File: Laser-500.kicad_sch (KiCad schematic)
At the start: 10 parts, among them Q1 9018G, U1 Z80CPU, U2 74LS257, U3 74LS257, U4 74LS244, U5 27128, U6 27128, U7 74LS273, U8 2764, U9 74LS00

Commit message: RAM4164
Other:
- added sheet RAM (ram.kicad_sch)
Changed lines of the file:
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@@
+		)
+	)
+	(sheet
+		(at 37.592 25.146)
+		(size 34.798 19.812)
+		(fields_autoplaced yes)
+		(stroke
+			(width 0.1524)
+			(type solid)
+		)
+		(fill
+			(color 0 0 0 0.0000)
+		)
+		(property "Sheetname" "RAM"
+			(at 37.592 24.4344 0)
+			(effects
+				(font
+					(size 1.27 1.27)
+				)
+				(justify left bottom)
+			)
+		)
+		(property "Sheetfile" "ram.kicad_sch"
+			(at 37.592 45.5426 0)
+			(effects
+				(font
+					(size 1.27 1.27)
+				)
+				(justify left top)
+			)
+		)
+		(instances
+			(project "Laser-500"
+				(path "/c1a6b1ae-77c2-4767-93cc-3749547878e9"
+					(page "2")
+				)
+			)
 		)
 	)

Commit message: First Draft - RAM
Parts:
- removed Q1: 9018G, symbol Device:Q_NPN_EBC
- removed U1: Z80CPU, symbol CPU:Z80CPU
- removed U2, U3: 74LS257, symbol 74xx:74LS257
- removed U4: 74LS244, symbol 74xx:74LS244
- removed U5, U6: 27128, Package_DIP:DIP-28_W15.24mm, symbol Memory_EPROM:27128
- removed U7: 74LS273, symbol 74xx:74LS273
- removed U8: 2764, Package_DIP:DIP-28_W15.24mm, symbol Memory_EPROM:2764
- removed U9: 74LS00, symbol 74xx:74LS00
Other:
- added sheet CPU and ROM (cpu_main.kicad_sch)

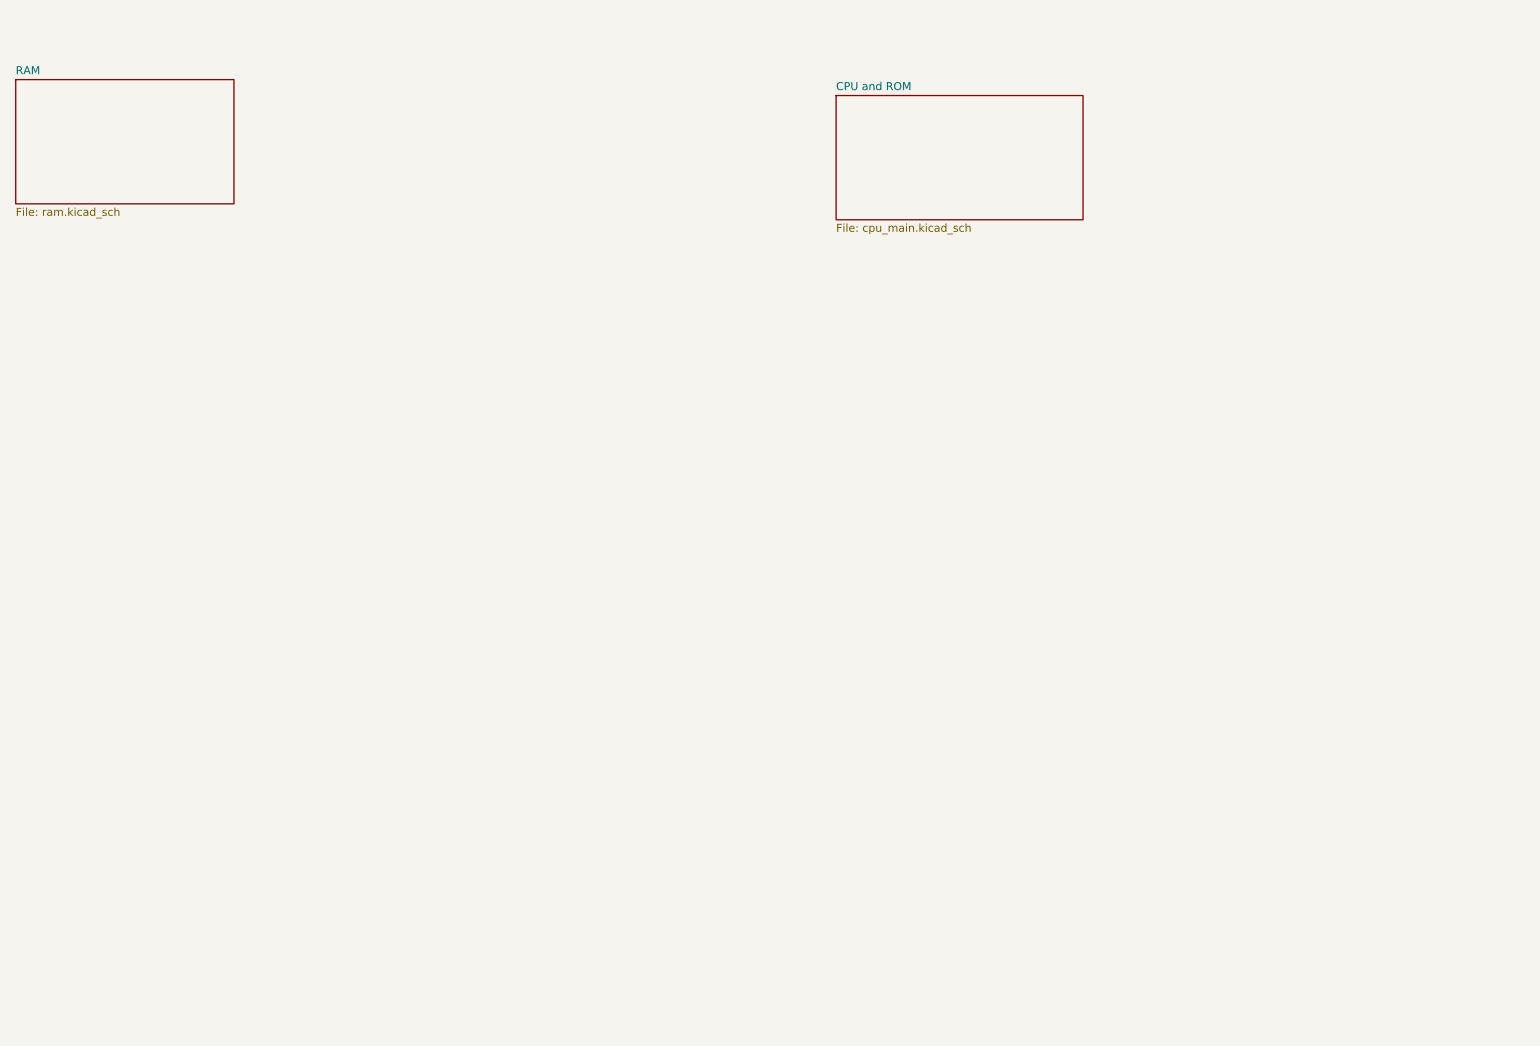
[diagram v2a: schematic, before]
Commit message: Started video_cassette sch
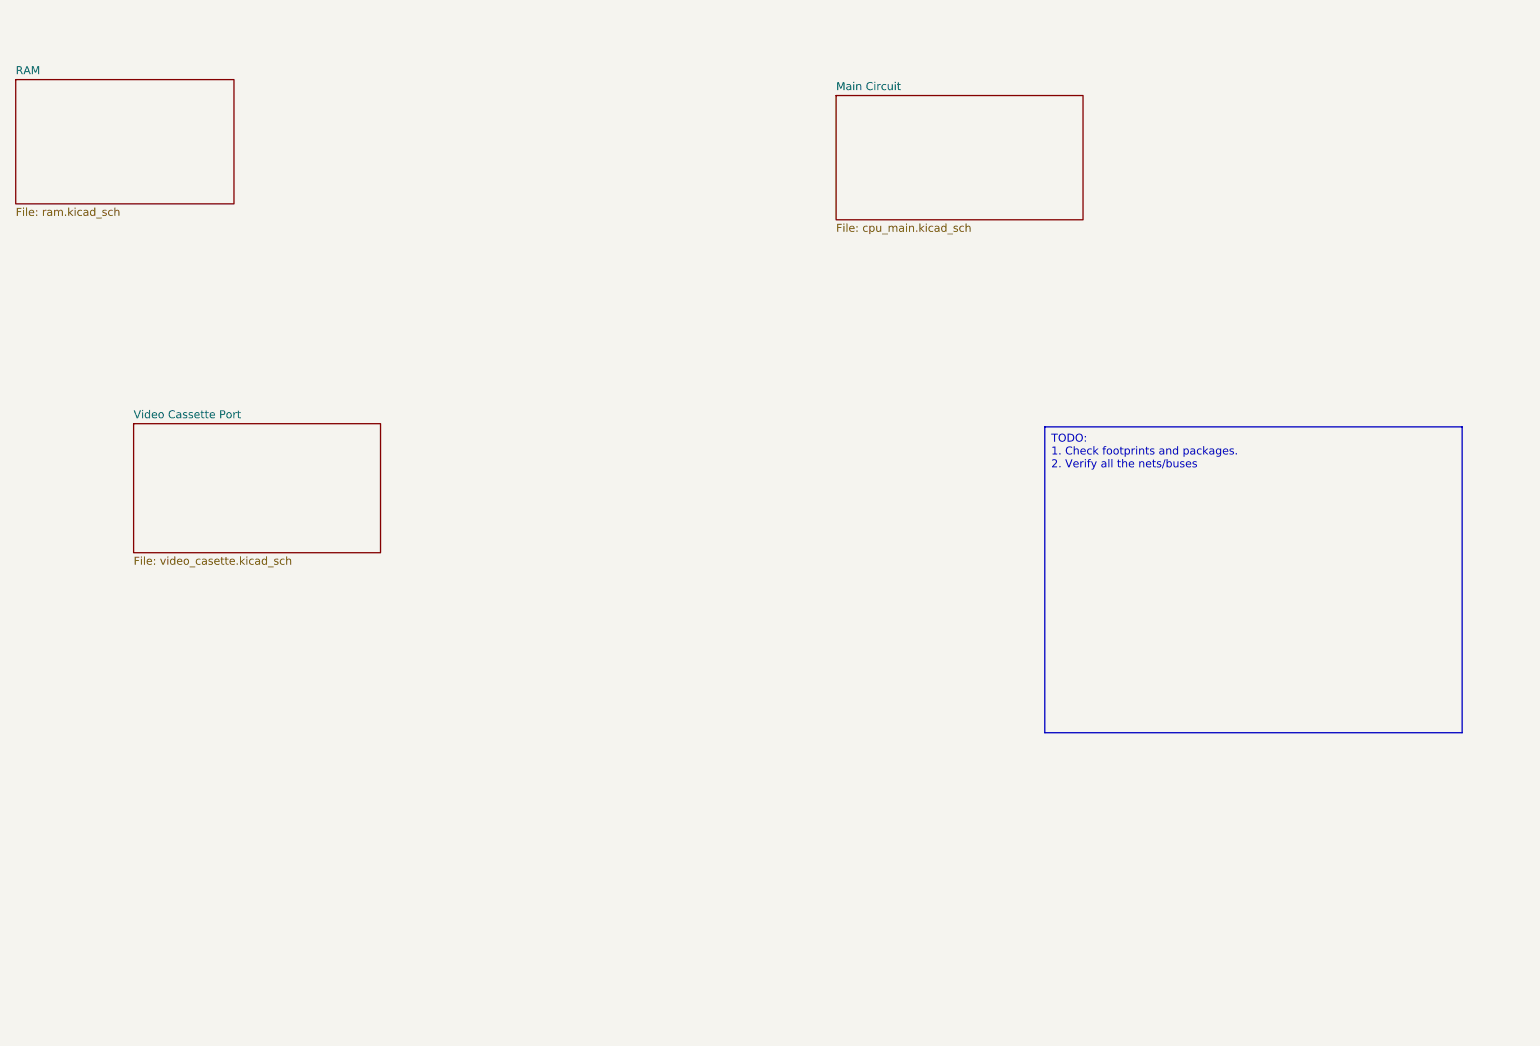
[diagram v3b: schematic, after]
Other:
- sheet CPU and ROM renamed Main Circuit
- added sheet Video Cassette Port (video_casette.kicad_sch)
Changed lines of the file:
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@@
 	(generator_version "8.0")
 	(paper "A4")
+	(text_box "TODO:\n1. Check footprints and packages.\n2. Verify all the nets/buses"
+		(exclude_from_sim no)
+		(at 201.676 80.518 0)
+		(size 66.548 48.768)
+		(stroke
+			(width 0)
+			(type default)
+		)
+		(fill
+			(type none)
+		)
+		(effects
+			(font
+				(size 1.27 1.27)
+			)
+			(justify left top)
+		)
+	)
 	(sheet
 		(at 37.592 25.146)
@@
 	)
 	(sheet
+		(at 56.388 80.01)
+		(size 39.37 20.574)
+		(fields_autoplaced yes)
+		(stroke
+			(width 0.1524)
+			(type solid)
+		)
+		(fill
+			(color 0 0 0 0.0000)
+		)
+		(property "Sheetname" "Video Cassette Port"
+			(at 56.388 79.2984 0)
+			(effects
+				(font
+					(size 1.27 1.27)
+				)
+				(justify left bottom)
+			)
+		)
+		(property "Sheetfile" "video_casette.kicad_sch"
+			(at 56.388 101.1686 0)
+			(effects
+				(font
+					(size 1.27 1.27)
+				)
+				(justify left top)
+			)
+		)
+		(instances
+			(project "Laser-500"
+				(path "/c1a6b1ae-77c2-4767-93cc-3749547878e9"
+					(page "4")
+				)
+			)
+		)
+	)
+	(sheet
 		(at 168.402 27.686)
 		(size 39.37 19.812)
@@
 			(color 0 0 0 0.0000)
 		)
-		(property "Sheetname" "CPU and ROM"
+		(property "Sheetname" "Main Circuit"
 			(at 168.402 26.9744 0)
 			(effects

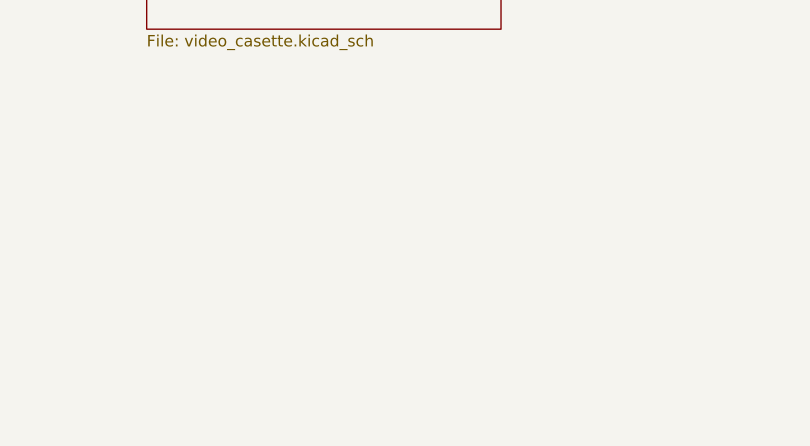
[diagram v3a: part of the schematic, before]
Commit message: A few Boxing day updates
1. Add Laser 500 Mainboard PCB photo
2. Updated Main circuit ICs and their symbols.
3. Updated references according to PCB photo
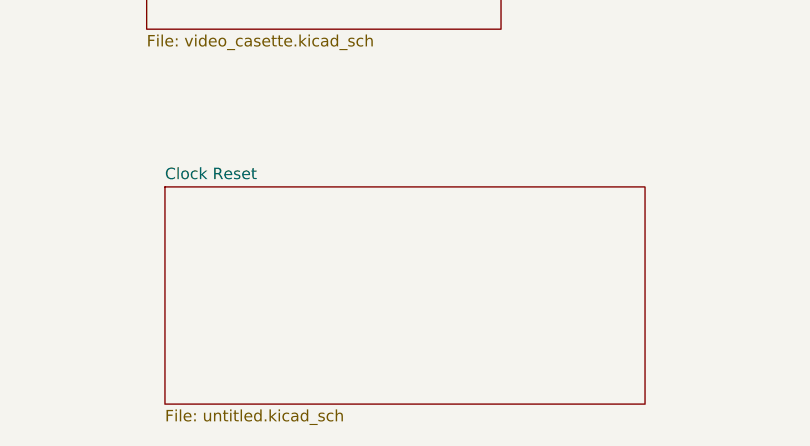
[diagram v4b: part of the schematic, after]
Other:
- added sheet Clock Reset (untitled.kicad_sch)
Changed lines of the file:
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@@
+	)
+	(sheet
+		(at 58.42 118.11)
+		(size 53.34 24.13)
+		(fields_autoplaced yes)
+		(stroke
+			(width 0.1524)
+			(type solid)
+		)
+		(fill
+			(color 0 0 0 0.0000)
+		)
+		(property "Sheetname" "Clock Reset"
+			(at 58.42 117.3984 0)
+			(effects
+				(font
+					(size 1.27 1.27)
+				)
+				(justify left bottom)
+			)
+		)
+		(property "Sheetfile" "untitled.kicad_sch"
+			(at 58.42 142.8246 0)
+			(effects
+				(font
+					(size 1.27 1.27)
+				)
+				(justify left top)
+			)
+		)
+		(instances
+			(project "Laser-500"
+				(path "/c1a6b1ae-77c2-4767-93cc-3749547878e9"
+					(page "5")
+				)
+			)
+		)
 	)
 	(sheet

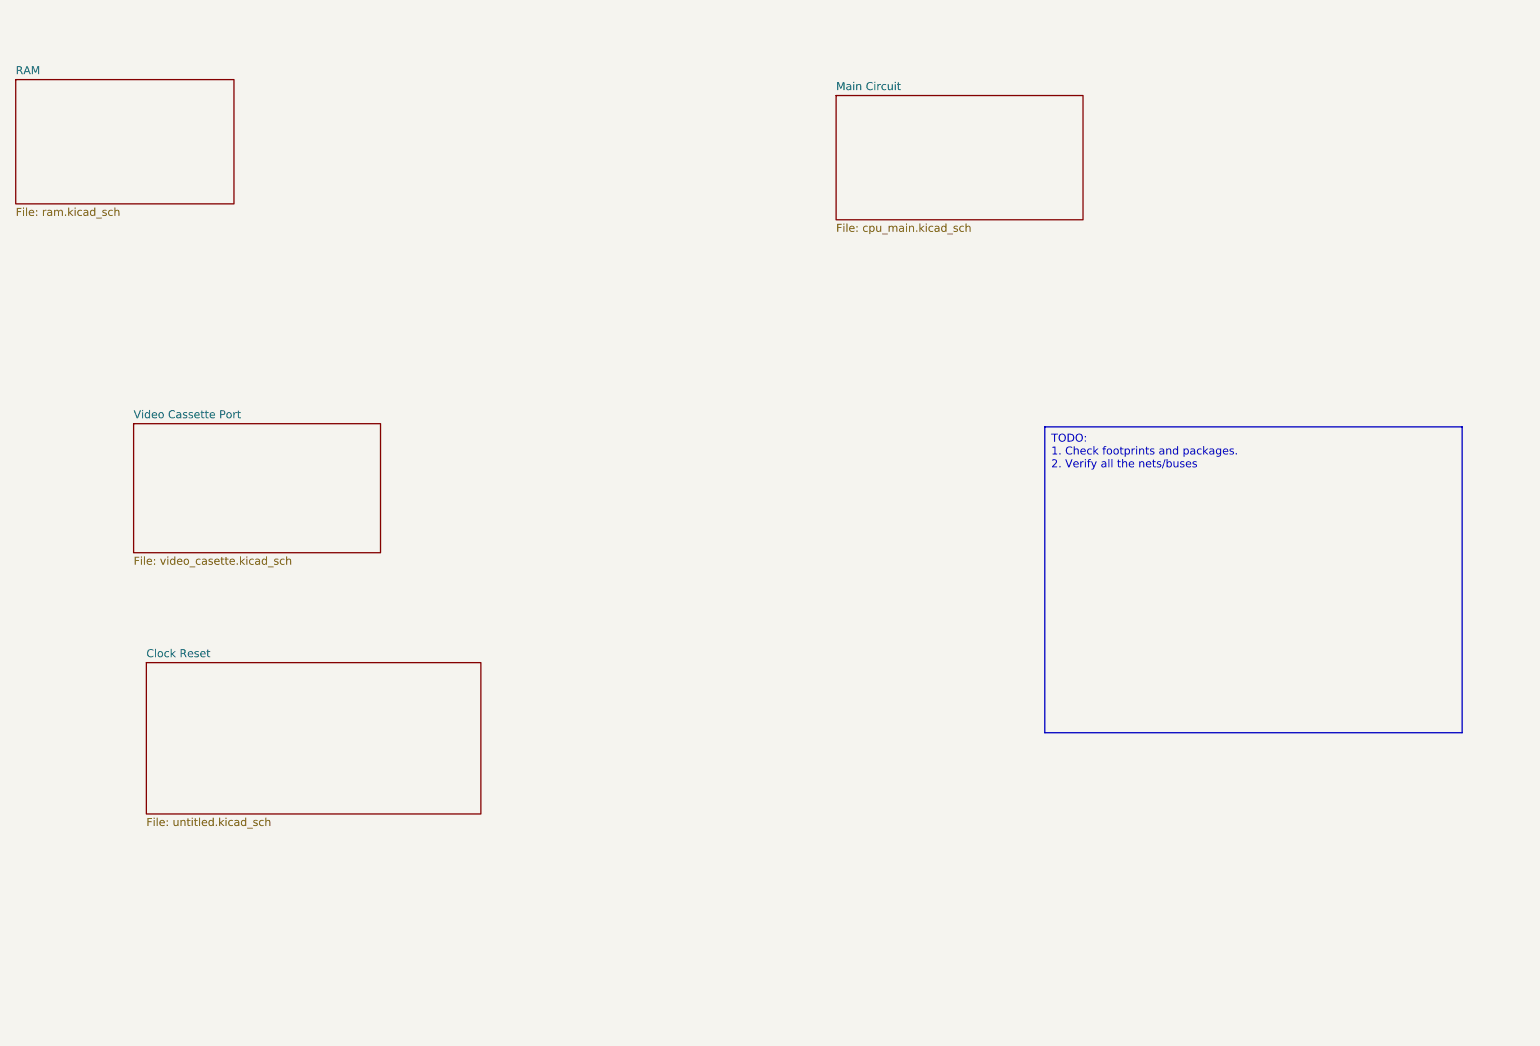
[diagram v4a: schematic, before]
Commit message: Started A[0..15] and MA[0..7] on main circuit
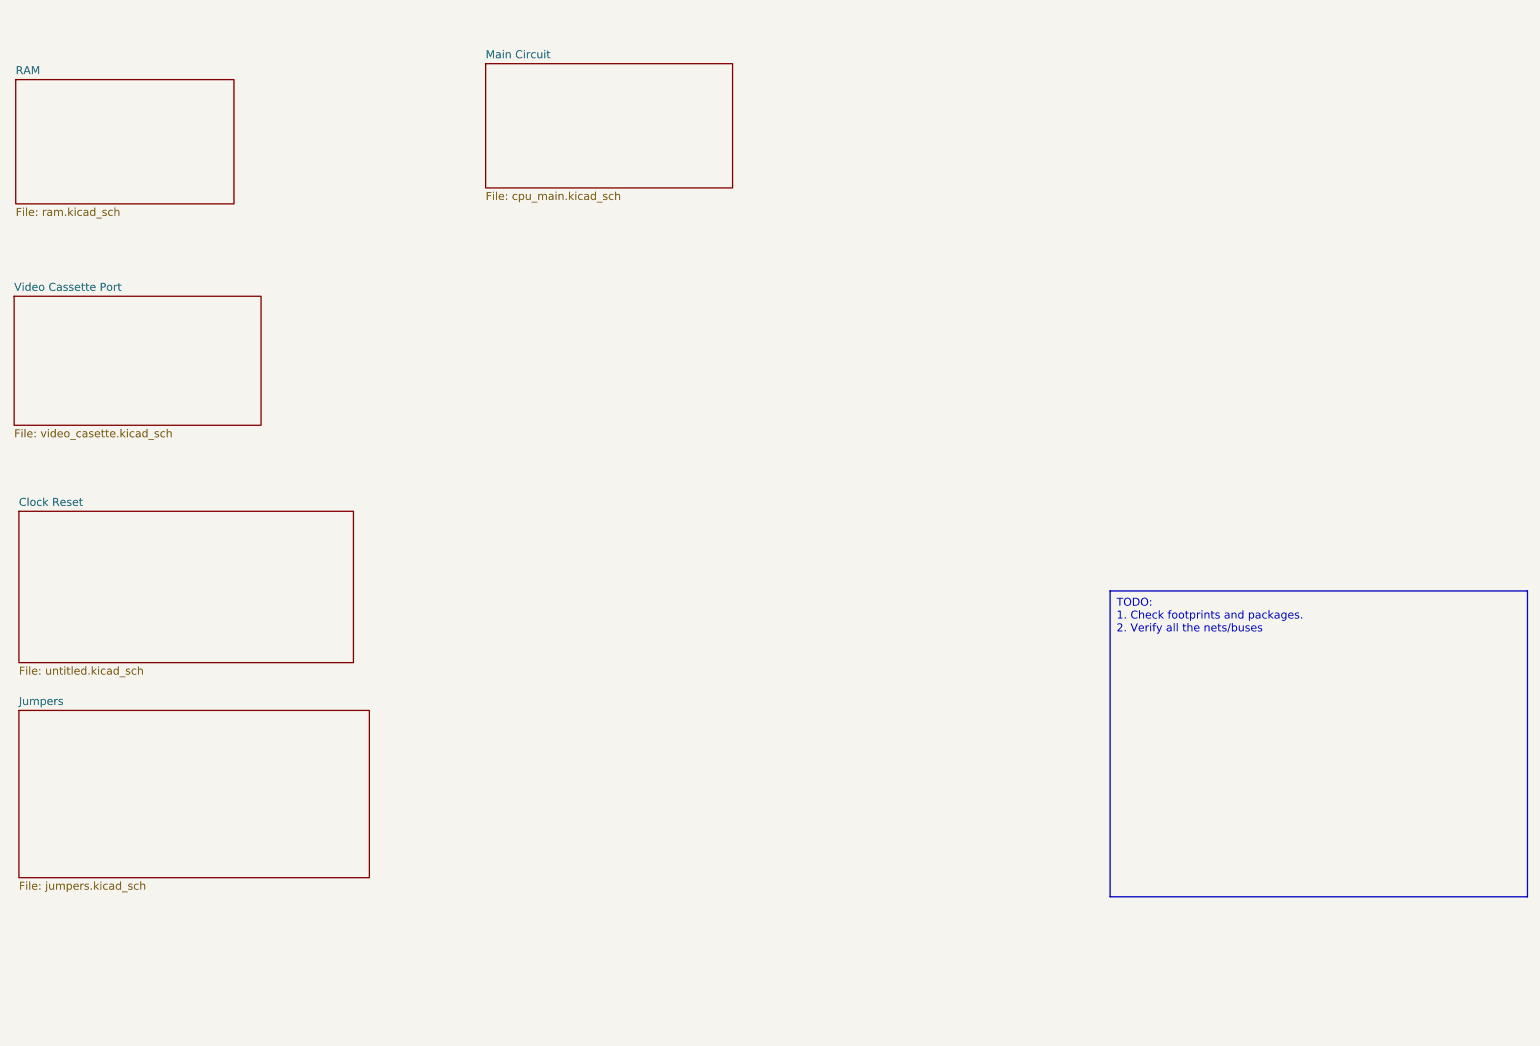
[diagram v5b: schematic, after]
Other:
- added sheet Jumpers (jumpers.kicad_sch)
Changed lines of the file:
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@@
 	(text_box "TODO:\n1. Check footprints and packages.\n2. Verify all the nets/buses"
 		(exclude_from_sim no)
-		(at 201.676 80.518 0)
+		(at 212.09 106.68 0)
 		(size 66.548 48.768)
 		(stroke
@@
 	)
 	(sheet
-		(at 58.42 118.11)
+		(at 38.1 93.98)
 		(size 53.34 24.13)
 		(fields_autoplaced yes)
@@
 		)
 		(property "Sheetname" "Clock Reset"
-			(at 58.42 117.3984 0)
+			(at 38.1 93.2684 0)
 			(effects
 				(font
@@
 		)
 		(property "Sheetfile" "untitled.kicad_sch"
-			(at 58.42 142.8246 0)
+			(at 38.1 118.6946 0)
 			(effects
 				(font
@@
 				(path "/c1a6b1ae-77c2-4767-93cc-3749547878e9"
 					(page "5")
+				)
+			)
+		)
+	)
+	(sheet
+		(at 38.1 125.73)
+		(size 55.88 26.67)
+		(fields_autoplaced yes)
+		(stroke
+			(width 0.1524)
+			(type solid)
+		)
+		(fill
+			(color 0 0 0 0.0000)
+		)
+		(property "Sheetname" "Jumpers"
+			(at 38.1 125.0184 0)
+			(effects
+				(font
+					(size 1.27 1.27)
+				)
+				(justify left bottom)
+			)
+		)
+		(property "Sheetfile" "jumpers.kicad_sch"
+			(at 38.1 152.9846 0)
+			(effects
+				(font
+					(size 1.27 1.27)
+				)
+				(justify left top)
+			)
+		)
+		(instances
+			(project "Laser-500"
+				(path "/c1a6b1ae-77c2-4767-93cc-3749547878e9"
+					(page "6")
 				)
 			)
@@
 	)
 	(sheet
-		(at 56.388 80.01)
+		(at 37.338 59.69)
 		(size 39.37 20.574)
 		(fields_autoplaced yes)
@@
 		)
 		(property "Sheetname" "Video Cassette Port"
-			(at 56.388 79.2984 0)
+			(at 37.338 58.9784 0)
 			(effects
 				(font
@@
 		)
 		(property "Sheetfile" "video_casette.kicad_sch"
-			(at 56.388 101.1686 0)
+			(at 37.338 80.8486 0)
 			(effects
 				(font
@@
 	)
 	(sheet
-		(at 168.402 27.686)
+		(at 112.522 22.606)
 		(size 39.37 19.812)
 		(fields_autoplaced yes)
@@
 		)
 		(property "Sheetname" "Main Circuit"
-			(at 168.402 26.9744 0)
+			(at 112.522 21.8944 0)
 			(effects
 				(font
@@
 		)
 		(property "Sheetfile" "cpu_main.kicad_sch"
-			(at 168.402 48.0826 0)
+			(at 112.522 43.0026 0)
 			(effects
 				(font

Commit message: End of vacation
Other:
- sheet Jumpers ports: added J2:~{TOPBK}; removed none
- sheet Main Circuit ports: added A[0..15], B, BUZZER, G, J2:~{TOPBK}, L, MA[0..7], R, RD[0..7], ~{RAS}; removed none
- sheet RAM ports: added MA[0..7], RD[0..7], ~{CAS}, ~{RAMW}, ~{RAS}; removed none
- sheet Video Cassette Port ports: added B, G, L, R; removed none
